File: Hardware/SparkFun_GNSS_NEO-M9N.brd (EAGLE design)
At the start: 64.9 x 38 mm, 68 parts, among them J1 MICROMOD_STANDARD, U1 U-BLOX_NEO-M9N, U2 3.3V, U3 EEPROM, U4 74HC1G04

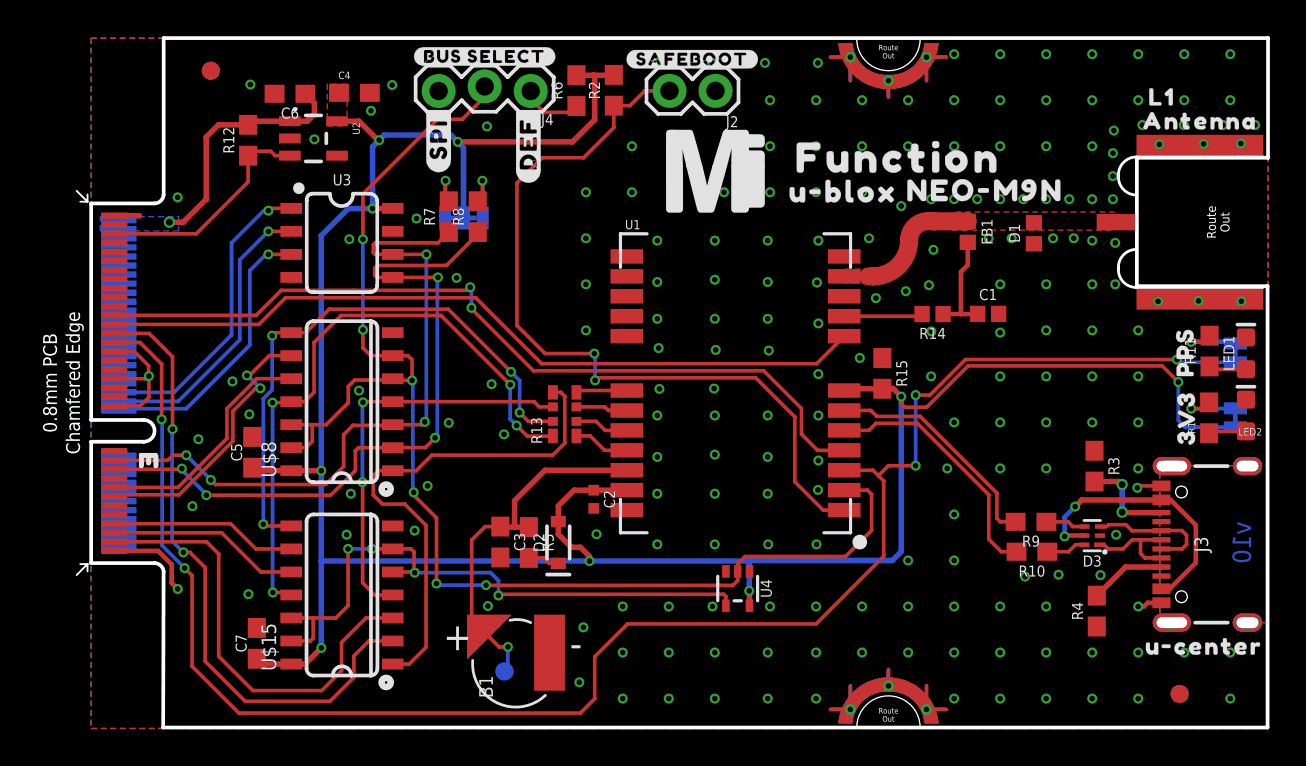
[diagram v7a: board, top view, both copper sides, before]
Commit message: Adds labels to bus selection jumper
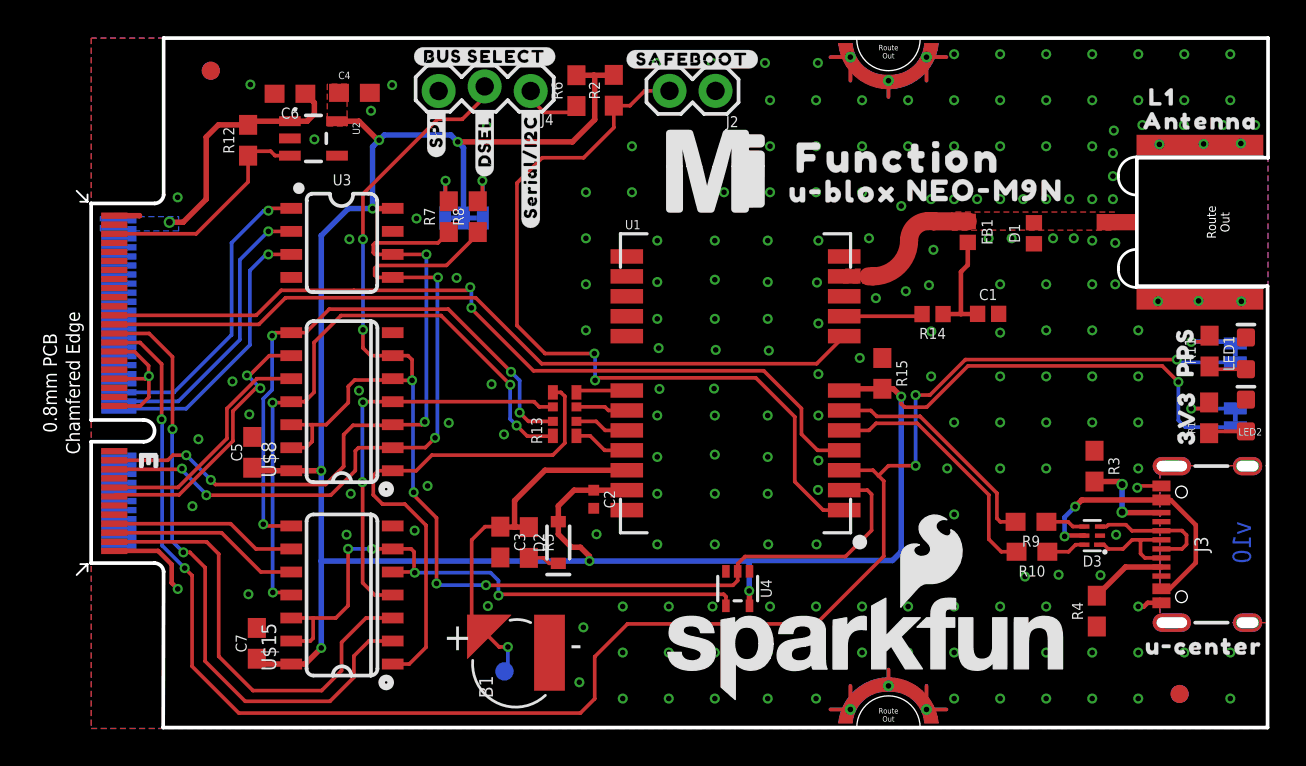
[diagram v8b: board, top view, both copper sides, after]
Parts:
- added U$19: (no value), top:#DSEL#40313522
- U$16: device top:#DEF#521 -> top:#SPI#40313521
- U$17: device top:#SPI#520 -> top:#SERIAL#I2C#40313523
- moved LOGO2 18.1 mm to (42.8, 4.42), flipped to the top
- moved U$17 5.30 mm to (24.3, 31.0)
- moved U$16 5.12 mm to (19.1, 32.9)
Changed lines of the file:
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@@
 <?xml version="1.0" encoding="utf-8"?>
 <!DOCTYPE eagle SYSTEM "eagle.dtd">
-<eagle version="9.5.1">
+<eagle version="9.6.2">
 <drawing>
 <settings>
@@
 <layer number="45" name="Holes" color="7" fill="1" visible="yes" active="yes"/>
 <layer number="46" name="Milling" color="3" fill="1" visible="no" active="yes"/>
-<layer number="47" name="Measures" color="7" fill="1" visible="yes" active="yes"/>
+<layer number="47" name="Measures" color="7" fill="1" visible="no" active="yes"/>
 <layer number="48" name="Document" color="7" fill="1" visible="no" active="yes"/>
 <layer number="49" name="Reference" color="13" fill="1" visible="yes" active="yes"/>
@@
 <layer number="115" name="ReferenceISLANDS" color="7" fill="1" visible="no" active="no"/>
 <layer number="116" name="Patch_BOT" color="9" fill="4" visible="no" active="no"/>
-<layer number="117" name="PM_Ref" color="26" fill="1" visible="no" active="yes"/>
+<layer number="117" name="PM_Ref" color="26" fill="1" visible="yes" active="yes"/>
 <layer number="118" name="Rect_Pads" color="7" fill="1" visible="no" active="no"/>
-<layer number="119" name="PF_Ref" color="31" fill="1" visible="no" active="yes"/>
-<layer number="120" name="WFL_Ref" color="25" fill="1" visible="no" active="yes"/>
+<layer number="119" name="PF_Ref" color="31" fill="1" visible="yes" active="yes"/>
+<layer number="120" name="WFL_Ref" color="25" fill="1" visible="yes" active="yes"/>
 <layer number="121" name="_tsilk" color="7" fill="1" visible="no" active="no"/>
 <layer number="122" name="_bsilk" color="7" fill="1" visible="no" active="no"/>
@@
 <attribute name="VALUE" x="35.727" y="37.219" size="0.6096" layer="27" font="vector" ratio="20" rot="R180"/>
 </element>
-<element name="LOGO2" library="SparkFun-Aesthetics" package="SFE_LOGO_NAME_FLAME_.2" value="SFE_LOGO_NAME_FLAME.2_INCH" x="35.687" y="21.0566" smashed="yes" rot="MR0"/>
+<element name="LOGO2" library="SparkFun-Aesthetics" package="SFE_LOGO_NAME_FLAME_.2" value="SFE_LOGO_NAME_FLAME.2_INCH" x="42.799" y="4.4196" smashed="yes"/>
 <element name="LOGO3" library="SparkFun-Aesthetics" package="OSHW-LOGO-S" value="OSHW-LOGOS" x="10.16" y="2.54" smashed="yes" rot="MR0"/>
 <element name="U$3" library="top" package="FUNCTION521" value="" x="44.5262" y="31.496" smashed="yes"/>
@@
 <attribute name="REV" value="" x="1.27" y="-39.37" size="1.778" layer="27" font="vector" ratio="15" display="off"/>
 </element>
-<element name="U$16" library="top" package="#DEF#521" value="" x="24.13" y="32.258" smashed="yes" rot="R90"/>
-<element name="U$17" library="top" package="#SPI#520" value="" x="19.177" y="32.512" smashed="yes" rot="R90"/>
 <element name="U$18" library="top" package="#BUS_SELECT#509" value="" x="21.717" y="37.084" smashed="yes"/>
+<element name="U$19" library="top" package="#DSEL#40313522" value="" x="21.717" y="32.385" smashed="yes" rot="R90"/>
+<element name="U$16" library="top" package="#SPI#40313521" value="" x="19.05" y="32.893" smashed="yes" rot="R90"/>
+<element name="U$17" library="top" package="#SERIAL#I2C#40313523" value="" x="24.257" y="30.988" smashed="yes" rot="R90"/>
 </elements>
 <signals>
